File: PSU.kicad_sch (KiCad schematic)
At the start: 10 parts

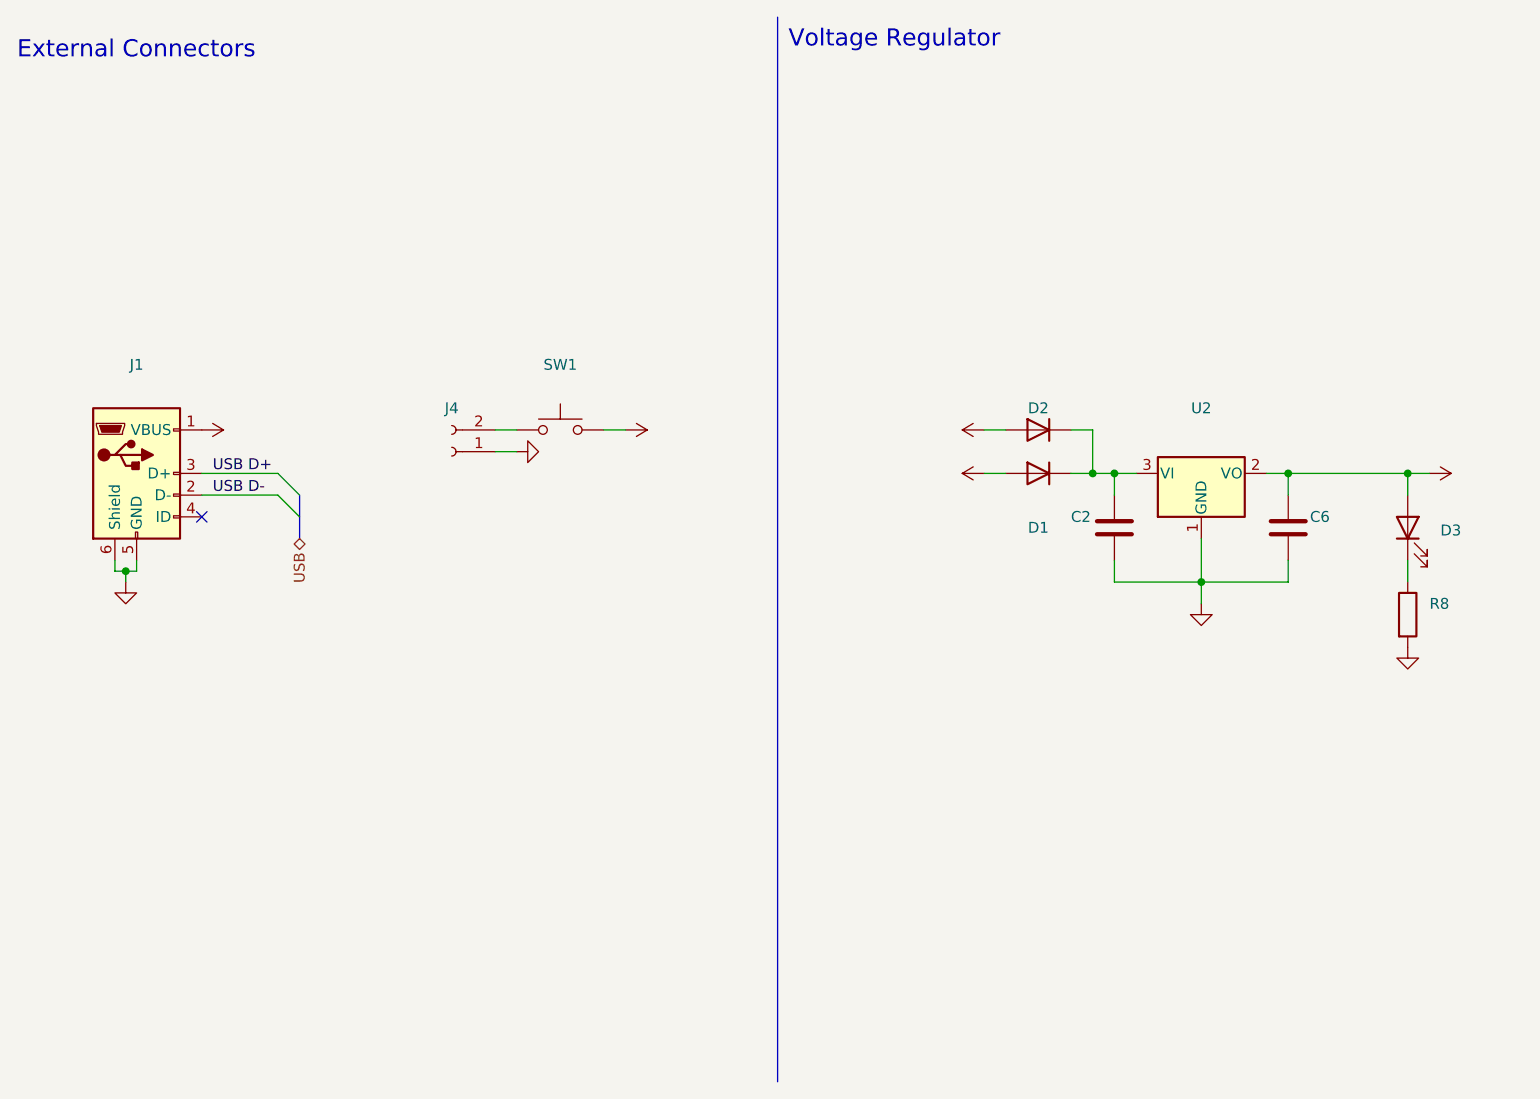
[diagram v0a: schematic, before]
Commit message: Added pullup resistors
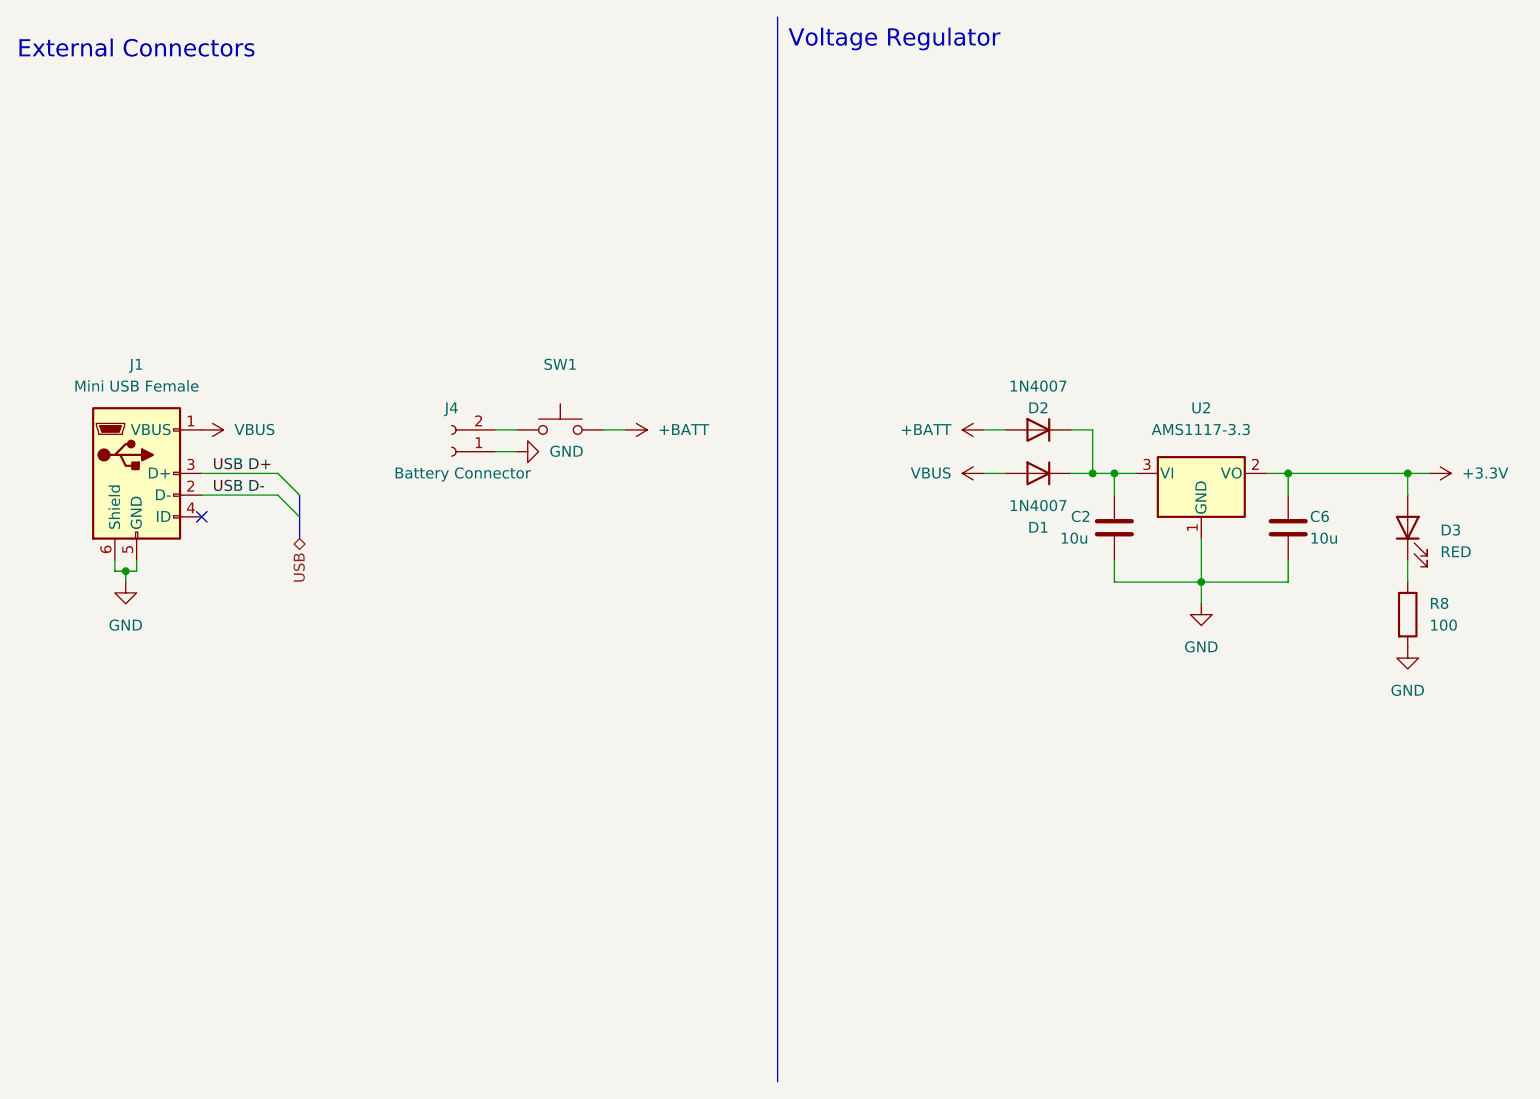
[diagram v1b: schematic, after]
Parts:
- C2, C6: value (none) -> 10u; footprint (none) -> Capacitor_SMD:C_0603_1608Metric
- D1, D2: value (none) -> 1N4007; footprint (none) -> Diode_SMD:D_SOD-123
- D3: value (none) -> RED; footprint (none) -> LED_THT:LED_D3.0mm
- J1: value (none) -> Mini USB Female; footprint (none) -> Connector_USB:USB_Mini-B_Lumberg_2486_01_Horizontal
- J4: value (none) -> Battery Connector; footprint (none) -> Connector_Wire:Compact_Relief
- R8: value (none) -> 100; footprint (none) -> Resistor_SMD:R_0603_1608Metric
- SW1: value (none) -> Screw Switch; footprint (none) -> Connector:Screw_Switch_M2
- U2: value (none) -> AMS1117-3.3; footprint (none) -> Package_TO_SOT_SMD:SOT-223-3_TabPin2
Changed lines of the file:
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@@
       (effects (font (size 1.27 1.27)) hide)
     )
-    (property "Value" "" (id 1) (at 181.61 64.7699 90)
+    (property "Value" "+3.3V" (id 1) (at 181.61 64.7699 90)
       (effects (font (size 1.27 1.27)) (justify left))
     )
@@
       (effects (font (size 1.27 1.27)) (justify right))
     )
-    (property "Value" "" (id 1) (at 179.07 73.9774 90)
-      (effects (font (size 1.27 1.27)) (justify right))
-    )
-    (property "Footprint" "" (id 2) (at 175.26 71.12 0)
+    (property "Value" "RED" (id 1) (at 179.07 73.9774 90)
+      (effects (font (size 1.27 1.27)) (justify right))
+    )
+    (property "Footprint" "LED_THT:LED_D3.0mm" (id 2) (at 175.26 71.12 0)
       (effects (font (size 1.27 1.27)) hide)
     )
@@
       (effects (font (size 1.27 1.27)) (justify right))
     )
-    (property "Value" "" (id 1) (at 134.62 72.39 0)
-      (effects (font (size 1.27 1.27)) (justify right))
-    )
-    (property "Footprint" "" (id 2) (at 140.0048 74.93 0)
+    (property "Value" "10u" (id 1) (at 134.62 72.39 0)
+      (effects (font (size 1.27 1.27)) (justify right))
+    )
+    (property "Footprint" "Capacitor_SMD:C_0603_1608Metric" (id 2) (at 140.0048 74.93 0)
       (effects (font (size 1.27 1.27)) hide)
     )
@@
       (effects (font (size 1.27 1.27)) hide)
     )
-    (property "Value" "" (id 1) (at 87.63 59.6899 90)
+    (property "Value" "+BATT" (id 1) (at 87.63 59.6899 90)
       (effects (font (size 1.27 1.27)) (justify left))
     )
@@
     (in_bom yes) (on_board yes) (fields_autoplaced)
     (property "Reference" "SW1" (id 0) (at 76.2 52.07 0))
-    (property "Value" "" (id 1) (at 76.2 54.61 0)
-      (effects (font (size 1.27 1.27)) hide)
-    )
-    (property "Footprint" "" (id 2) (at 76.2 54.61 0)
+    (property "Value" "Screw Switch" (id 1) (at 76.2 54.61 0)
+      (effects (font (size 1.27 1.27)) hide)
+    )
+    (property "Footprint" "Connector:Screw_Switch_M2" (id 2) (at 76.2 54.61 0)
       (effects (font (size 1.27 1.27)) hide)
     )
@@
     (in_bom yes) (on_board yes)
     (property "Reference" "J4" (id 0) (at 63.5 57.15 0))
-    (property "Value" "" (id 1) (at 64.77 64.77 0))
-    (property "Footprint" "" (id 2) (at 63.5 62.23 0)
+    (property "Value" "Battery Connector" (id 1) (at 64.77 64.77 0))
+    (property "Footprint" "Connector_Wire:Compact_Relief" (id 2) (at 63.5 62.23 0)
       (effects (font (size 1.27 1.27)) hide)
     )
@@
       (effects (font (size 1.27 1.27)) (justify right))
     )
-    (property "Value" "" (id 1) (at 163.83 72.39 0)
-      (effects (font (size 1.27 1.27)) (justify right))
-    )
-    (property "Footprint" "" (id 2) (at 160.3248 74.93 0)
+    (property "Value" "10u" (id 1) (at 163.83 72.39 0)
+      (effects (font (size 1.27 1.27)) (justify right))
+    )
+    (property "Footprint" "Capacitor_SMD:C_0603_1608Metric" (id 2) (at 160.3248 74.93 0)
       (effects (font (size 1.27 1.27)) hide)
     )
@@
       (effects (font (size 1.27 1.27)) hide)
     )
-    (property "Value" "" (id 1) (at 175.26 90.17 0))
+    (property "Value" "GND" (id 1) (at 175.26 90.17 0))
     (property "Footprint" "" (id 2) (at 175.26 85.09 0)
       (effects (font (size 1.27 1.27)) hide)
@@
       (effects (font (size 1.27 1.27)) hide)
     )
-    (property "Value" "" (id 1) (at 25.4 82.55 0))
+    (property "Value" "GND" (id 1) (at 25.4 82.55 0))
     (property "Footprint" "" (id 2) (at 25.4 77.47 0)
       (effects (font (size 1.27 1.27)) hide)
@@
       (effects (font (size 1.27 1.27)) hide)
     )
-    (property "Value" "" (id 1) (at 38.1 59.6899 90)
+    (property "Value" "VBUS" (id 1) (at 38.1 59.6899 90)
       (effects (font (size 1.27 1.27)) (justify left))
     )
@@
       (effects (font (size 1.27 1.27)) (justify left))
     )
-    (property "Value" "" (id 1) (at 177.8 82.5499 0)
-      (effects (font (size 1.27 1.27)) (justify left))
-    )
-    (property "Footprint" "" (id 2) (at 173.482 81.28 90)
+    (property "Value" "100" (id 1) (at 177.8 82.5499 0)
+      (effects (font (size 1.27 1.27)) (justify left))
+    )
+    (property "Footprint" "Resistor_SMD:R_0603_1608Metric" (id 2) (at 173.482 81.28 90)
       (effects (font (size 1.27 1.27)) hide)
     )
@@
       (effects (font (size 1.27 1.27)) hide)
     )
-    (property "Value" "" (id 1) (at 74.93 62.2299 90)
+    (property "Value" "GND" (id 1) (at 74.93 62.2299 90)
       (effects (font (size 1.27 1.27)) (justify right))
     )
@@
     (in_bom yes) (on_board yes) (fields_autoplaced)
     (property "Reference" "J1" (id 0) (at 26.67 52.07 0))
-    (property "Value" "" (id 1) (at 26.67 54.61 0))
-    (property "Footprint" "" (id 2) (at 30.48 66.04 0)
+    (property "Value" "Mini USB Female" (id 1) (at 26.67 54.61 0))
+    (property "Footprint" "Connector_USB:USB_Mini-B_Lumberg_2486_01_Horizontal" (id 2) (at 30.48 66.04 0)
       (effects (font (size 1.27 1.27)) hide)
     )
@@
     (in_bom yes) (on_board yes) (fields_autoplaced)
     (property "Reference" "D1" (id 0) (at 132.08 71.12 0))
-    (property "Value" "" (id 1) (at 132.08 68.58 0))
-    (property "Footprint" "" (id 2) (at 132.08 69.215 0)
+    (property "Value" "1N4007" (id 1) (at 132.08 68.58 0))
+    (property "Footprint" "Diode_SMD:D_SOD-123" (id 2) (at 132.08 69.215 0)
       (effects (font (size 1.27 1.27)) hide)
     )
@@
     (in_bom yes) (on_board yes)
     (property "Reference" "D2" (id 0) (at 132.08 57.15 0))
-    (property "Value" "" (id 1) (at 132.08 54.61 0))
-    (property "Footprint" "" (id 2) (at 132.08 64.135 0)
+    (property "Value" "1N4007" (id 1) (at 132.08 54.61 0))
+    (property "Footprint" "Diode_SMD:D_SOD-123" (id 2) (at 132.08 64.135 0)
       (effects (font (size 1.27 1.27)) hide)
     )
@@
       (effects (font (size 1.27 1.27)) hide)
     )
-    (property "Value" "" (id 1) (at 121.92 64.7701 90)
+    (property "Value" "VBUS" (id 1) (at 121.92 64.7701 90)
       (effects (font (size 1.27 1.27)) (justify left))
     )
@@
       (effects (font (size 1.27 1.27)) hide)
     )
-    (property "Value" "" (id 1) (at 151.13 85.09 0))
+    (property "Value" "GND" (id 1) (at 151.13 85.09 0))
     (property "Footprint" "" (id 2) (at 151.13 80.01 0)
       (effects (font (size 1.27 1.27)) hide)
@@
       (effects (font (size 1.27 1.27)) hide)
     )
-    (property "Value" "" (id 1) (at 121.92 59.6901 90)
+    (property "Value" "+BATT" (id 1) (at 121.92 59.6901 90)
       (effects (font (size 1.27 1.27)) (justify left))
     )
@@
     (in_bom yes) (on_board yes) (fields_autoplaced)
     (property "Reference" "U2" (id 0) (at 151.13 57.15 0))
-    (property "Value" "" (id 1) (at 151.13 59.69 0))
-    (property "Footprint" "" (id 2) (at 151.13 59.69 0)
-      (effects (font (size 1.27 1.27)) hide)
-    )
+    (property "Value" "AMS1117-3.3" (id 1) (at 151.13 59.69 0))
+    (property "Footprint" "Package_TO_SOT_SMD:SOT-223-3_TabPin2" (id 2) (at 151.13 59.69 0)
+      (effects (font (size 1.27 1.27)) hide)
+    )

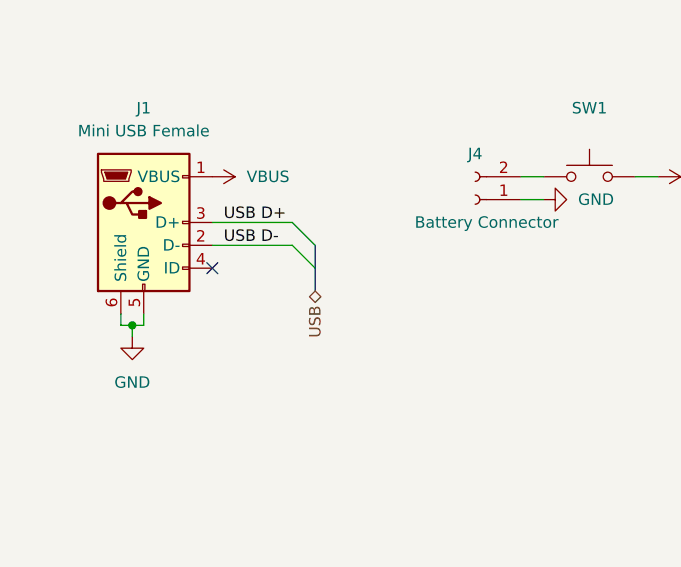
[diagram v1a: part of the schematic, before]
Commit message: Fixed bus names
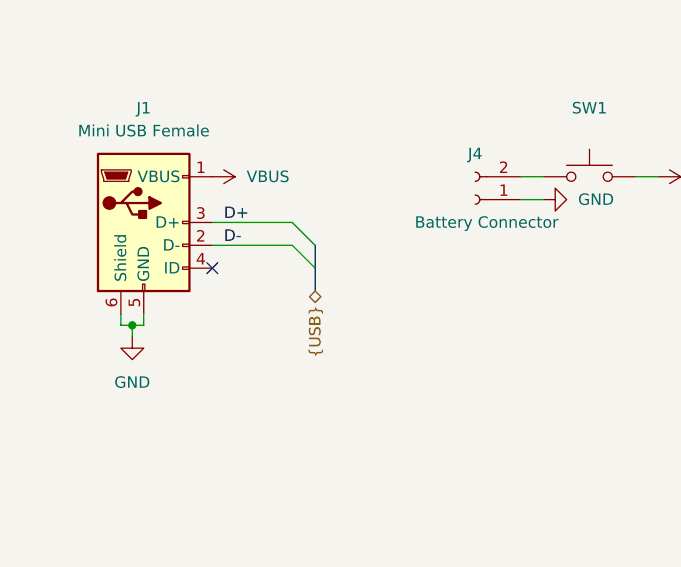
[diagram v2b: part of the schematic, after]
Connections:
- net USB D+ renamed D+
- net USB D- renamed D-
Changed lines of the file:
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@@
     (effects (font (size 2 2)) (justify left bottom))
   )
-  (label "USB D-" (at 35.56 67.31 0)
+  (label "D-" (at 35.56 67.31 0)
     (effects (font (size 1.27 1.27)) (justify left bottom))
   )
-  (label "USB D+" (at 35.56 64.77 0)
+  (label "D+" (at 35.56 64.77 0)
     (effects (font (size 1.27 1.27)) (justify left bottom))
   )
-  (hierarchical_label "USB" (shape bidirectional) (at 45.72 72.39 270)
+  (hierarchical_label "{USB}" (shape bidirectional) (at 45.72 72.39 270)
     (effects (font (size 1.27 1.27)) (justify right))
   )

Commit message: Various updates because I forgot to commit for a while
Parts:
- removed SW1: Screw Switch, Connector:Screw_Switch_M2, symbol Switch:SW_Push
- added R8: 33k, symbol Device:R
- added R9: 12k, symbol Device:R
- J2: renamed from J4; footprint Connector_Wire:Compact_Relief -> Connector_Phoenix_MC_HighVoltage:PhoenixContact_MCV_1,5_4-G-5.08_1x04_P5.08mm_Vertical; symbol Connector:Conn_01x02_Female -> Connector:Conn_01x04_Female
- renumbered C2 to C12, C6 to C13, D2 to D1, D1 to D2, R8 to R10, U2 to U3
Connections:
- net +BATT: now also J2.1 (Pin_1), R8.1
- net GND: now also J2.4 (Pin_4), R9.2; no longer J2.1 (Pin_1)
- net VBat in: now reaches J2.2 (Pin_2)
- net VBat in: now also J2.3 (Pin_3)
- new net VBat/4: R8.2, R9.1
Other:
- moved on the sheet: J1
